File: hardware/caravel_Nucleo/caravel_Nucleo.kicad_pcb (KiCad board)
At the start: 2 copper layers, 68.1 x 92.5 mm, 82 parts, among them J1 USB4105-GF-A, J10 PinHeader_1x11, J11 PinHeader_1x02, J12 PinHeader_1x02, J2 M20-9990246, J3 PinHeader_1x02, J4 61300411121, J5 PinHeader_1x02, J6 PinHeader_1x02, J7 61300611121, J8 640456-3, J9 640456-3, SW1 KMR2, T1 Logo, T2 Logo, U1 FT232HQ, U12 NUCLEO144-F429ZI, U2 SN74LVC1G125DCKR, U3 SN74LVC1G125DCKR, U4 MAX811REUS+T, U5 MCP4661-103E/ML, U6 Caravel_breakout_PCB, U7 W25Q32FVSS, U9 MIC2211-AAYML-TR, X1 ECS-2520MVLC-100-BN-TR, Y1 ABM8G-12.000MHZ-18-D2Y-T

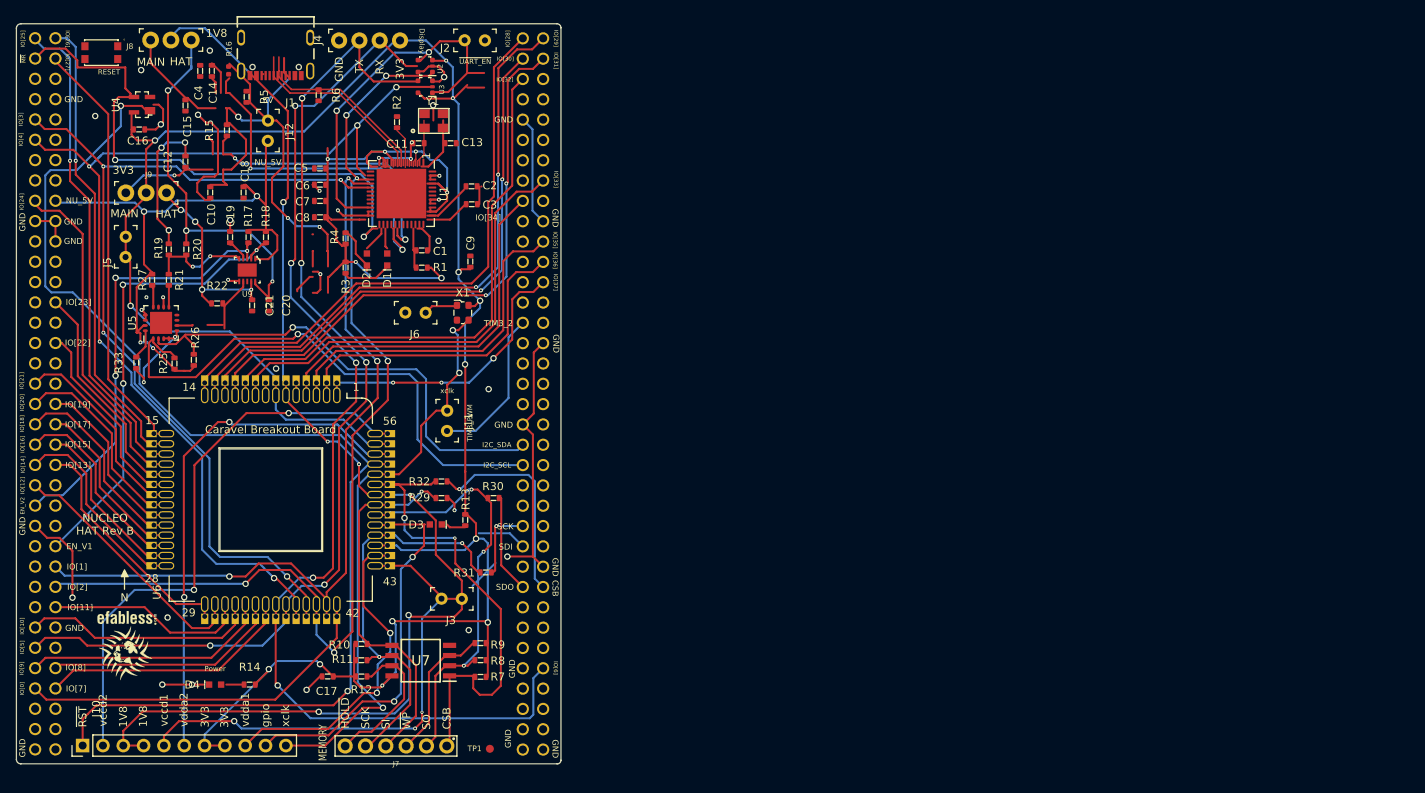
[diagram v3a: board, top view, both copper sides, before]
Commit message: Initial PCB placement, start routing
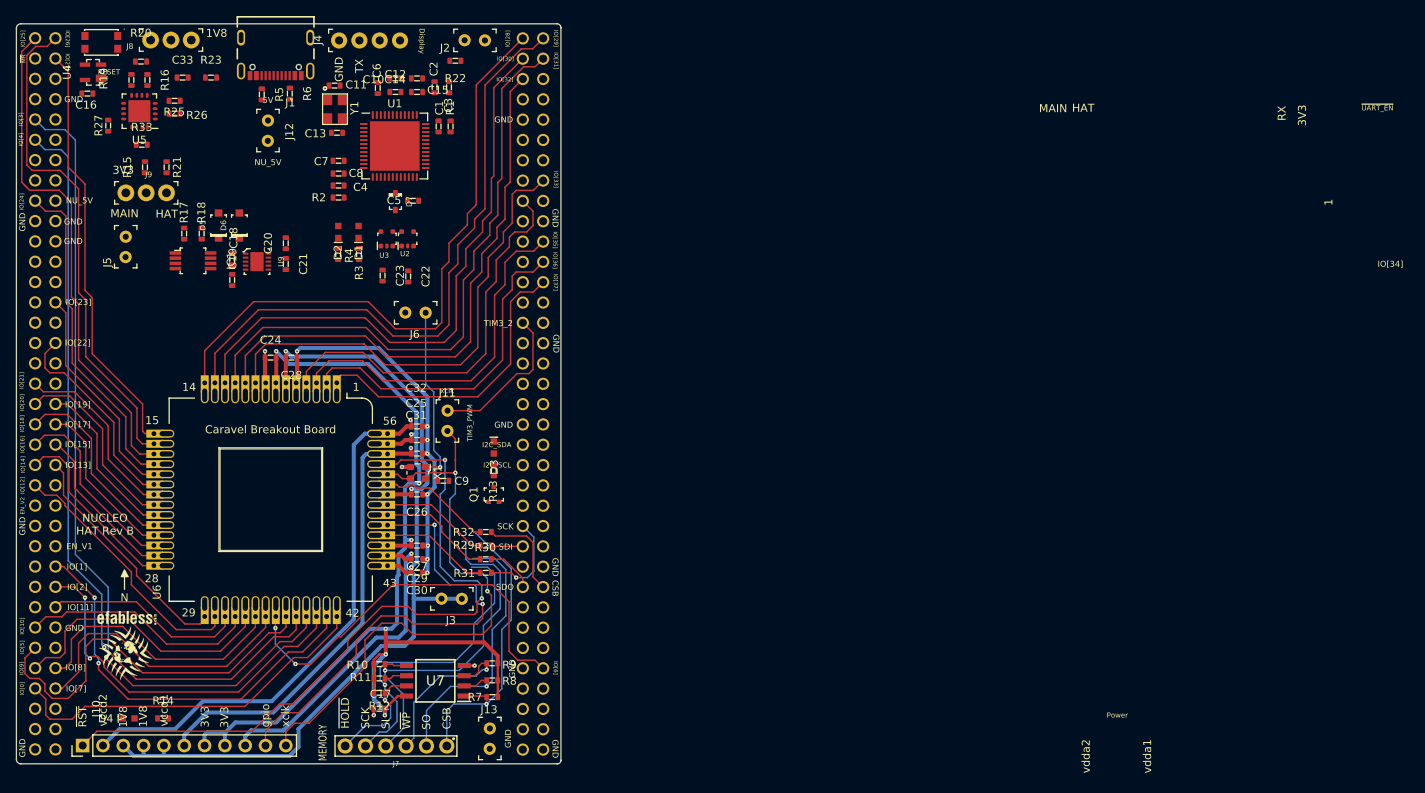
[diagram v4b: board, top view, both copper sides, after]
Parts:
- removed TP1: TP_SMD1MM, antmicro-footprints:Testpoint_smd_1mm
- added C22: C_100n_0603, antmicro-footprints:0603-cap, F.Cu at (149.0, 48.9)
- added C23: C_100n_0603, antmicro-footprints:0603-cap, F.Cu at (145.8, 48.8)
- added C24: C_100n_0603, antmicro-footprints:0603-cap, F.Cu at (131.8, 59.1)
- added C25: C_100n_0603, antmicro-footprints:0603-cap, F.Cu at (150.1, 69.4)
- added C26: C_100n_0603, antmicro-footprints:0603-cap, F.Cu at (150.1, 76.2)
- added C27: C_100n_0603, antmicro-footprints:0603-cap, F.Cu at (150.1, 82.6)
- added C28: C_100n_0603, antmicro-footprints:0603-cap, F.Cu at (134.4, 59.1)
- added C29: C_100n_0603, antmicro-footprints:0603-cap, F.Cu at (150.1, 84.3)
- added C30: C_100n_0603, antmicro-footprints:0603-cap, F.Cu at (150.1, 86.0)
- added C31: C_100n_0603, antmicro-footprints:0603-cap, F.Cu at (150.1, 71.1)
- added C32: C_100n_0603, antmicro-footprints:0603-cap, F.Cu at (150.1, 67.7)
- added C33: C_1u_0603, antmicro-footprints:0603-cap, F.Cu at (120.8, 24.1)
- added D5: 1N5819HW-7-F, antmicro-footprints:SOD-123, F.Cu at (125.3, 42.6)
- added D6: 1N5819HW-7-F, antmicro-footprints:SOD-123, F.Cu at (127.9, 42.6)
- added D7: PMEG6002EJ,115, antmicro-footprints:SOD-323F, F.Cu at (147.4, 39.6)
- added IC1: 74LVC2G32DP,125, antmicro-footprints:TSSOP-8_W3mm, F.Cu at (122.1, 47.0)
- added J13: PinHeader_1x02, antmicro-footprints:PinHeader_1x2_P2.54mm, F.Cu at (159.2, 105.5)
- added Q1: BSS84AKW, antmicro-footprints:SOT-323, F.Cu at (159.7, 76.2)
- added R23: R_10k_0603, antmicro-footprints:0603-res, F.Cu at (124.3, 24.1)
- R16: value R_34k_0402 -> R_34k_0603; footprint antmicro-footprints:0402-res -> antmicro-footprints:0603-res
- moved R22 42.5 mm to (154.9, 22.0), turned to 180 degrees
- moved R25 32.8 mm to (119.8, 27.0), turned to 0 degrees
- moved R26 30.9 mm to (119.8, 28.6), turned to 0 degrees
- moved C15 29.0 mm to (150.1, 25.9), turned to 180 degrees
- moved C12 27.6 mm to (147.4, 25.9), turned to 0 degrees
- moved C9 27.6 mm to (153.4, 74.5), turned to 180 degrees
- moved R33 27.3 mm to (115.7, 32.5), turned to 0 degrees
- moved C10 27.2 mm to (147.4, 24.2), turned to 180 degrees
- moved U5 26.6 mm to (115.4, 28.3), turned to 180 degrees
- moved C14 25.7 mm to (150.1, 24.2), turned to 0 degrees
- moved R20 23.7 mm to (115.6, 22.1), turned to 0 degrees
- moved C4 22.5 mm to (140.3, 37.6), turned to 180 degrees
- moved R19 22.3 mm to (114.4, 24.4)
- moved U2 21.7 mm to (148.9, 44.3), turned to 0 degrees
- moved X1 20.8 mm to (150.2, 73.5), turned to -90 degrees
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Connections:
- C18 pad 1: Net-(C18-Pad1) -> +5V
- R17 pad 2: Net-(C18-Pad1) -> +5V
- R18 pad 2: Net-(C18-Pad1) -> +5V
- R25 pad 2: Net-(C18-Pad1) -> +5V
- R26 pad 2: Net-(C18-Pad1) -> +5V
- R27 pad 1: Net-(C18-Pad1) -> +5V
- U1 pad 12: (no net) -> /FTDI_3V3
- U1 pad 21: /~{UART_EN} -> Net-(U1-Pad21)
- U1 pad 24: (no net) -> /FTDI_3V3
- U1 pad 29: /EN_1V8 -> /EN_1V8_FTDI
- U1 pad 3: (no net) -> /FTDI_3V3
- U1 pad 30: /EN_3V3 -> /EN_3V3_FTDI
- U1 pad 46: (no net) -> /FTDI_3V3
- U1 pad 8: (no net) -> /FTDI_3V3
- U12 pad 47: /EN_VOUT2 -> /EN_1V8_STM
- U12 pad 52: /EN_VOUT1 -> /EN_3V3_STM
- U5 pad 15: Net-(C18-Pad1) -> +5V
- U9 pad 1: Net-(C18-Pad1) -> +5V
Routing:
- net +3V3: track 399.5 -> 138.0 mm, vias 20 -> 7
- net AGND: track 226.1 -> 57.1 mm, vias 27 -> 12
- net ~{RST}: track 154.8 -> 0.00 mm, vias 2 -> 0
- net +1V8: track 248.0 -> 115.9 mm, vias 16 -> 3
- net /UART8_RX: track 148.2 -> 50.1 mm, vias 5 -> 2
- net /FTDI_3V3: track 92.7 -> 0.00 mm, vias 6 -> 0
- net /~{RST}: track 0.00 -> 88.4 mm, vias 0 -> 2
- net /SPI5_MOSI: track 130.8 -> 47.4 mm, vias 6 -> 2
- net Net-(C18-Pad1): track 83.3 -> 0.00 mm, vias 4 -> 0
- net /UART8_TX: track 129.6 -> 49.2 mm, vias 5 -> 0
- net (no net): track 69.6 -> 0.00 mm, vias 7 -> 0
- net /~{MR}: track 69.3 -> 0.00 mm, vias 2 -> 0
- net /I2C4_SCL: track 68.9 -> 0.00 mm, vias 1 -> 0
- net /I2C4_SDA: track 60.5 -> 0.00 mm, vias 1 -> 0
- net /EN_VOUT1: track 57.6 -> 0.00 mm, vias 3 -> 0
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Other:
- copper layers 2 -> 4

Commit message: Route FTDI and corresponding interfaces, route dynamic power supply, connect remainig signals
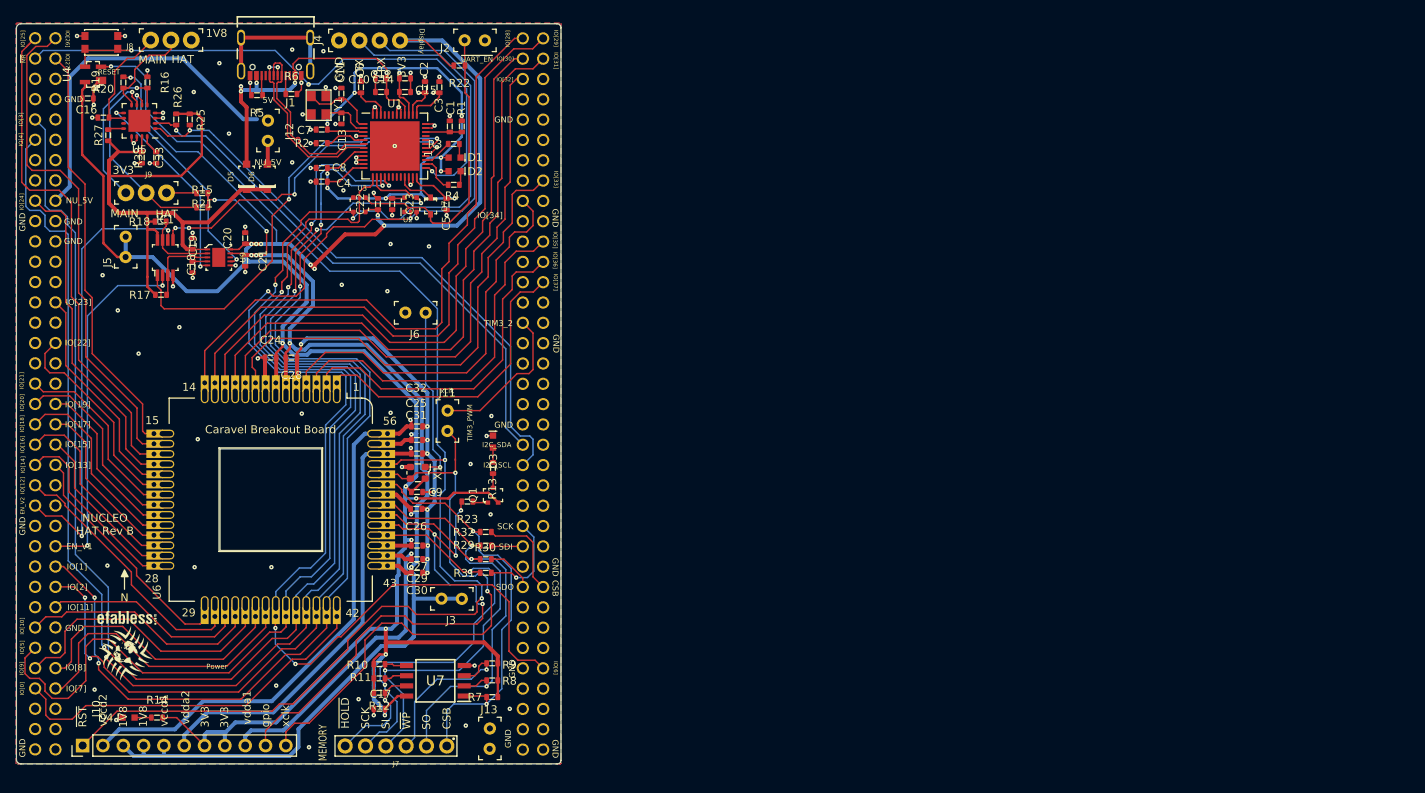
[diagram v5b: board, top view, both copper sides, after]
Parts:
- moved R23 61.9 mm to (156.4, 77.1), turned to 180 degrees
- moved R3 18.2 mm to (154.7, 32.4), turned to 0 degrees
- moved R4 16.9 mm to (154.7, 37.5), turned to 0 degrees
- moved D2 16.4 mm to (154.8, 35.8), turned to 180 degrees
- moved D1 15.2 mm to (154.8, 34.1), turned to 180 degrees
- moved C33 11.2 mm to (115.7, 34.1), turned to -90 degrees
- moved C22 9.80 mm to (145.2, 39.9), turned to 90 degrees
- moved C23 9.03 mm to (147.0, 39.9)
- moved R15 8.74 mm to (123.2, 40.3), turned to 0 degrees
- moved R20 8.43 mm to (110.9, 29.1)
- moved R17 8.18 mm to (118.1, 51.2), turned to 180 degrees
- moved R2 7.12 mm to (138.2, 32.3)
- moved D5 7.03 mm to (128.8, 36.5)
- moved D6 7.03 mm to (131.4, 36.5)
- moved R21 5.51 mm to (123.2, 38.5), turned to 0 degrees
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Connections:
- C23 pad 1: +3V3 -> /FTDI_3V3
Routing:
- net +3V3: track 138.0 -> 336.9 mm, vias 7 -> 16
- net /UART8_TX: track 49.2 -> 167.9 mm, vias 0 -> 2
- net /UART8_RX: track 50.1 -> 167.3 mm, vias 2 -> 4
- net /FTDI_3V3: track 0.00 -> 99.2 mm, vias 0 -> 10
- net /SPI5_MOSI: track 47.4 -> 130.9 mm, vias 2 -> 5
- net /~{MR}: track 0.00 -> 82.6 mm, vias 0 -> 2
- net /SPI5_CS: track 103.5 -> 184.4 mm, vias 1 -> 4
- net /SPI5_SCK: track 98.0 -> 176.7 mm, vias 1 -> 2
- net /SPI5_MISO: track 50.9 -> 129.1 mm, vias 2 -> 5
- net +5V: track 0.00 -> 77.0 mm
- net /~{RST}: track 88.4 -> 164.8 mm, vias 2 -> 3
- net /I2C4_SCL: track 0.00 -> 74.2 mm, vias 0 -> 1
- net /I2C4_SDA: track 0.00 -> 68.8 mm, vias 0 -> 1
- net AGND: track 57.1 -> 114.8 mm, vias 12 -> 89
- net /EN_1V8_STM: track 0.00 -> 56.5 mm, vias 0 -> 2
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- added copper zone on B.Cu, net AGND
- added copper zone on F.Cu, net AGND

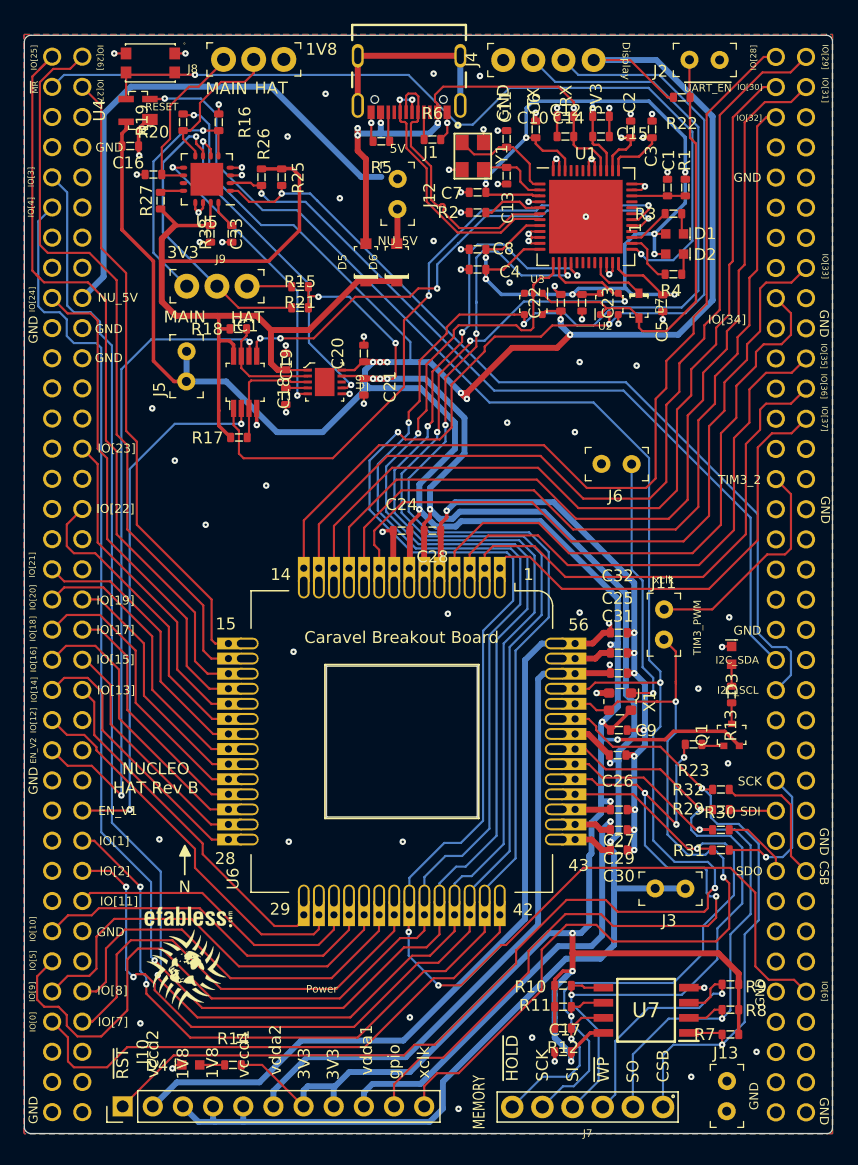
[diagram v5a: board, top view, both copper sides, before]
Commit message: Finish routing PCB, add I2C logic level translator, fix layer stackup, clear DRC, tidy up silkscreen
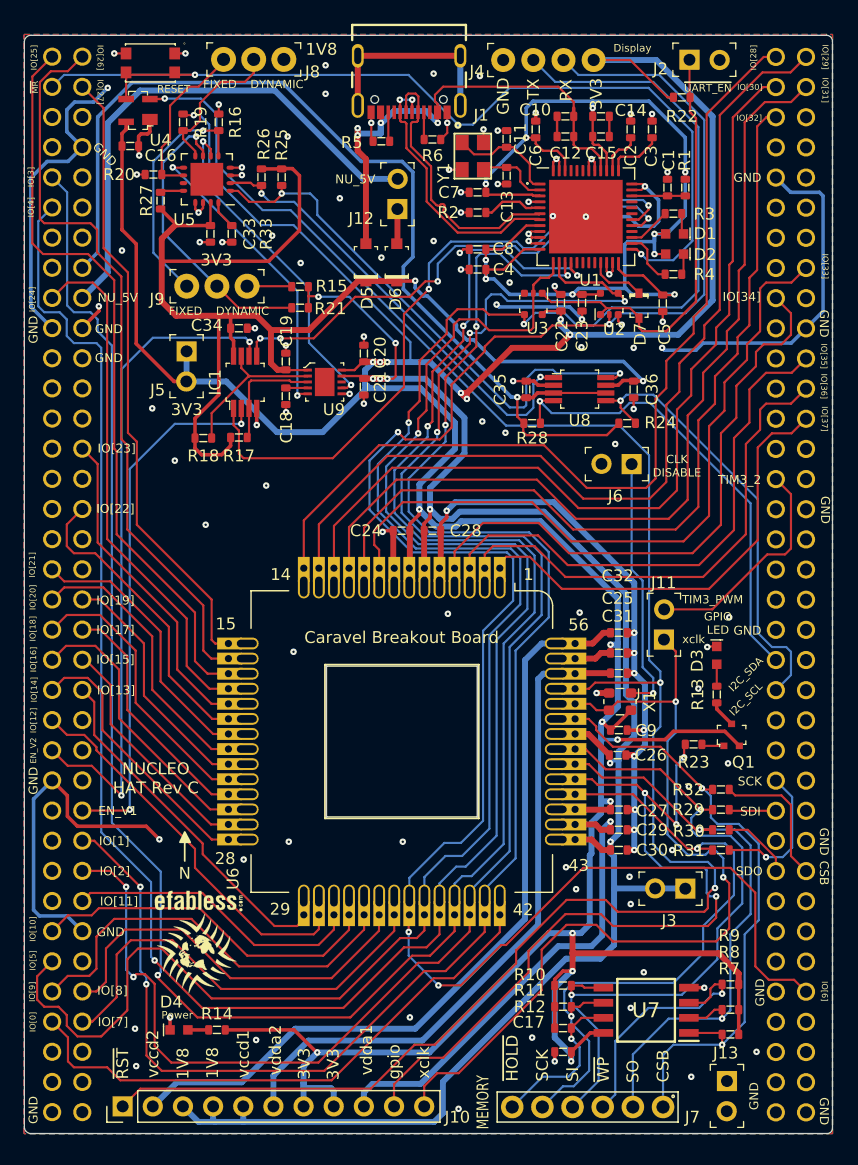
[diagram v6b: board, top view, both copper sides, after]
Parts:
- added C34: C_100n_0603, antmicro-footprints:0603-cap, F.Cu at (118.1, 42.0)
- added C35: C_100n_0603, antmicro-footprints:0603-cap, F.Cu at (142.3, 47.2)
- added C36: C_100n_0603, antmicro-footprints:0603-cap, F.Cu at (151.3, 47.2)
- added R24: R_4k7_0603, antmicro-footprints:0603-res, F.Cu at (150.8, 50.0)
- added R28: R_4k7_0603, antmicro-footprints:0603-res, F.Cu at (142.8, 50.0)
- added U8: NTS0102DP, antmicro-footprints:TSSOP-8_W3mm, F.Cu at (146.8, 47.2)
- C33: value C_1u_0603 -> C_100n_0603
- J2: value M20-9990246 -> PinHeader_1x02
- moved R18 9.66 mm to (115.1, 51.3)
- moved R14 3.24 mm to (116.2, 101.2)
- moved D4 3.11 mm to (113.0, 101.2)
- moved J12 2.54 mm to (131.5, 32.0), turned to 90 degrees
- moved J2 2.54 mm to (156.1, 19.4), turned to 0 degrees
- moved T1 1.60 mm to (114.5, 94.7)
- moved T2 1.60 mm to (114.7, 90.3)
- moved D3 1.25 mm to (158.3, 69.6)
- moved R13 1.25 mm to (158.3, 72.9)
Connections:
- D6 pad A: /NU_5V -> /NU_5V_JMPR
- J12 pad 1: +5V -> /NU_5V_JMPR
- J2 pad 1: AGND -> /~{UART_EN}
- J2 pad 2: /~{UART_EN} -> AGND
- U12 pad 113: /I2C4_SDA -> /I2C4_SDA_3V3
- U12 pad 115: /I2C4_SCL -> /I2C4_SCL_3V3
- U12 pad 16: unconnected-(U12-Pad16) -> /NU_3V3
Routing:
- net AGND: track 114.8 -> 224.2 mm, vias 89 -> 112
- net /NU_3V3: track 0.00 -> 87.1 mm, vias 0 -> 1
- net /I2C4_SDA_3V3: track 0.00 -> 39.1 mm, vias 0 -> 1
- net /I2C4_SCL_3V3: track 0.00 -> 37.5 mm, vias 0 -> 1
- net +5V: track 77.0 -> 110.9 mm, vias 0 -> 2
- net /I2C4_SDA: track 68.8 -> 38.2 mm, vias 1 -> 2
- net /I2C4_SCL: track 74.2 -> 46.5 mm, vias 1 -> 2
- net /SPI5_MOSI: track 130.9 -> 138.4 mm
- net +3V3: track 336.9 -> 342.6 mm, vias 16 -> 17
- net /SPI5_MISO: track 129.1 -> 134.2 mm
- net /EN_VOUT1: track 9.38 -> 13.5 mm
- net /NU_5V_JMPR: track 0.00 -> 2.94 mm
- net /mprj_io[24]: track 41.1 -> 43.9 mm
- net /NU_5V: track 46.7 -> 44.3 mm
- net /mprj_io[25]: track 65.0 -> 62.8 mm
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- added copper zone on In1.Cu, net AGND
- added copper zone on In2.Cu, net AGND
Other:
- board text added: "CLK DISABLE"
- board text added: "DYNAMIC"
- board text added: "FIXED"
- board text added: "GPIO LED"
- board text added: "NUCLEO HAT Rev C"
- board text removed: "5V"
- board text removed: "HAT"
- board text removed: "MAIN"
- board text removed: "NUCLEO HAT Rev B"
